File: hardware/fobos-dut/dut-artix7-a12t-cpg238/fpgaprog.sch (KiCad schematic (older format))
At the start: 42 parts, among them J7 0878321420, SW1 SW_DIP_x03, U1 XC7A12T-CPG238

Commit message: Started to rewire the CPG238 into the schematic Split FPGA Power and Programming into two sheets since new FPGA symbol explicitly displays each power pin and is much larger
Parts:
- removed C25: 100uF, Capacitor_SMD:C_1210_3225Metric_Pad1.33x2.70mm_HandSolder, symbol Device:C
- removed C26, C27, C35: 47uF, Capacitor_SMD:C_0603_1608Metric_Pad1.08x0.95mm_HandSolder, symbol Device:C
- removed C28, C29, C36, C37, C38, C39, C40, C41: 4.7uF, Capacitor_SMD:C_0402_1005Metric_Pad0.74x0.62mm_HandSolder, symbol Device:C
- removed C30, C31, C32, C33, C34, C42, C43, C44, C45, C46, C47, C48, C49, C50, C51, C52, C53: .47uF, Capacitor_SMD:C_0402_1005Metric_Pad0.74x0.62mm_HandSolder, symbol Device:C
- U1: footprint (none) -> Package_BGA:Xilinx_CPG238
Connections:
- wire segments 220 -> 106
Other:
- note removed: "BANK0\nE10, R10"
- note removed: "BANK14\nL16, P17, R14, T11, U8, U18, V15"
- note removed: "BANK15\nA16, B13, C10, D17, E14, G18, H15"
- note removed: "BANK34\nL6, M3, P7, R4, T1, V5"
- moved on the sheet: U1B

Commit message: Connected the fixed signals to the FPGA, flexible IO are left unconnected Added 0.1 ohm resistors to the 1V8 and 3V3 power rails, added test points which allow for easy measurement Updated ARTIX7-A12T-CPG238 symbol to make schematic route similarly to the last symbol Connected CFGVBS signal to the 3V3 rail, was previously connected to VCCINT which was a mistake Ran through 7 Series schematic review checklist - 7_Series_Schematic_Review_Recommendations.xlsm Added Xilinx pinout files for the CPG238 package Generated schematic for the csg325 for easy referencing
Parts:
- removed S2: 1825910-6, cerg:Switch_Tactile_THT_6x6mm, symbol cerg:1825910-6
- added C37: 47uF, Capacitor_SMD:C_0603_1608Metric_Pad1.08x0.95mm_HandSolder, symbol Device:C
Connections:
- net labels removed: VCCINT
- wire segments 106 -> 90
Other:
- note added: "BANK0\nG12, V11"
- moved on the sheet: D6, R29, R31, R32, R33, R53, R54, R55, R72, SW1, U1B

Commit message: Added SMA-JOHNSON-142-0701-201 Vertical SMA footprint to CERG lib, added this footprint to the Vcore measurement Re-positioned Power circuitry to the top right quadrant Re-positioned FOBOS connector to the center on the left edge of the board Re-positioned JTAG Connector, Mode switch, and gain control switch to the top left quadrant of the board
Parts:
- J7: symbol dk_Rectangular-Connectors-Headers-Male-Pins:0878321420 -> Connector_Generic:Conn_02x07_Odd_Even
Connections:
- net labels added: MODE_1
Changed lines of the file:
@@
 Connection ~ 3750 4550
 Wire Wire Line
-	4450 4450 4450 4400
-Wire Wire Line
 	5050 4650 5050 4250
 Wire Wire Line
@@
 	5250 4850 5250 4350
 $Comp
-L dk_Rectangular-Connectors-Headers-Male-Pins:0878321420 J?
+L Connector_Generic:Conn_02x07_Odd_Even J?
 U 1 1 600F5844
 P 4100 4750
@@
 Wire Wire Line
 	3750 5050 3900 5050
-Wire Wire Line
-	4300 4850 5250 4850
-Wire Wire Line
-	4300 4750 5150 4750
-Wire Wire Line
-	4300 4650 5050 4650
-Wire Wire Line
-	4300 4450 4450 4450
 $Comp
 L cerg:SW_DIP_x03 SW1
@@
 	5150 4450 5900 4450
 Wire Wire Line
-	5900 4550 4300 4550
-Wire Wire Line
 	5350 4650 5900 4650
 Wire Wire Line
@@
 	1    0    0    -1
 $EndComp
+Text Label 5450 3950 0    50   ~ 0
+MODE_1
+Wire Wire Line
+	4400 4450 4450 4450
+Wire Wire Line
+	4450 4450 4450 4400
+Wire Wire Line
+	4400 4550 5900 4550
+Wire Wire Line
+	5050 4650 4400 4650
+Wire Wire Line
+	5150 4750 4400 4750
+Wire Wire Line
+	5250 4850 4400 4850
 $EndSCHEMATC

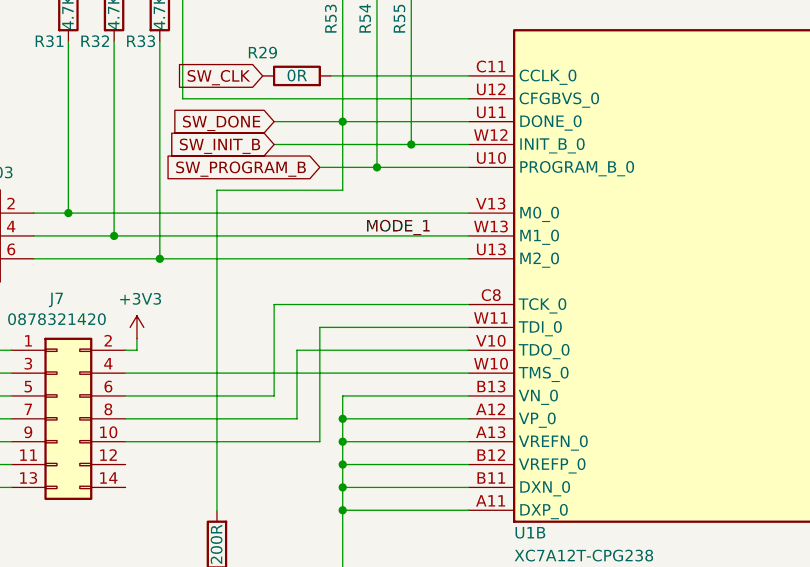
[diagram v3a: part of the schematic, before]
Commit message: updated library ref for diode and FET, placed target connector and some parts
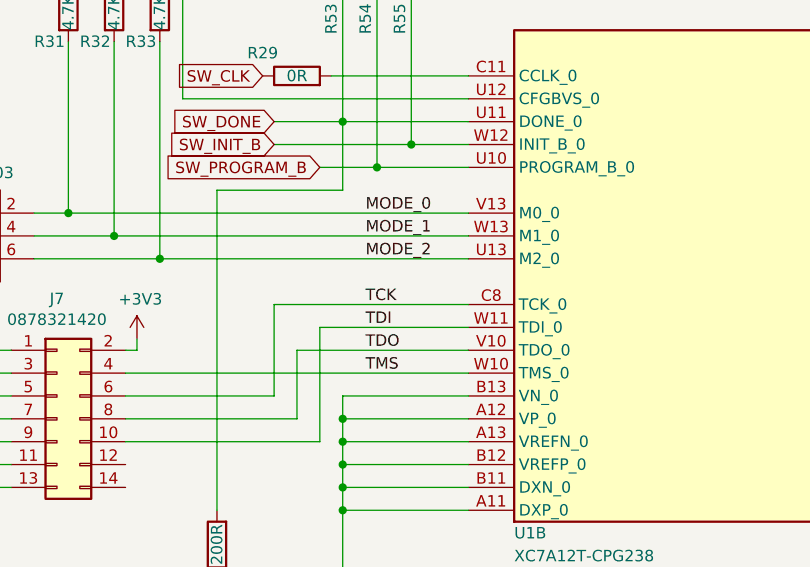
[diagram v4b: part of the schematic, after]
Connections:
- net MODE_2: now reaches R33.2, SW1.6, U1.U13 (M2_0)
- net MODE_0: now reaches R31.2, SW1.2, U1.V13 (M0_0)
- net TDI: now reaches J7.10 (Pin_10), U1.W11 (TDI_0)
- net TMS: now reaches J7.4 (Pin_4), U1.W10 (TMS_0)
- net TCK: now reaches J7.6 (Pin_6), U1.C8 (TCK_0)
- net TDO: now reaches J7.8 (Pin_8), U1.V10 (TDO_0)
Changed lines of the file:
@@
 Wire Wire Line
 	5250 4850 4400 4850
+Text Label 5450 3850 0    50   ~ 0
+MODE_0
+Text Label 5450 4050 0    50   ~ 0
+MODE_2
+Text Label 5450 4250 0    50   ~ 0
+TCK
+Text Label 5450 4350 0    50   ~ 0
+TDI
+Text Label 5450 4450 0    50   ~ 0
+TDO
+Text Label 5450 4550 0    50   ~ 0
+TMS
 $EndSCHEMATC

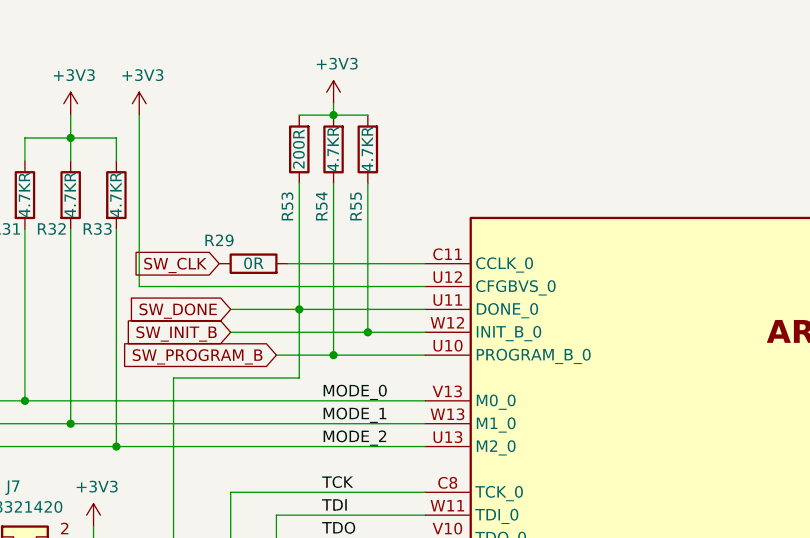
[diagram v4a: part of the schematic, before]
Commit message: few layout alignments incl space around FPGA
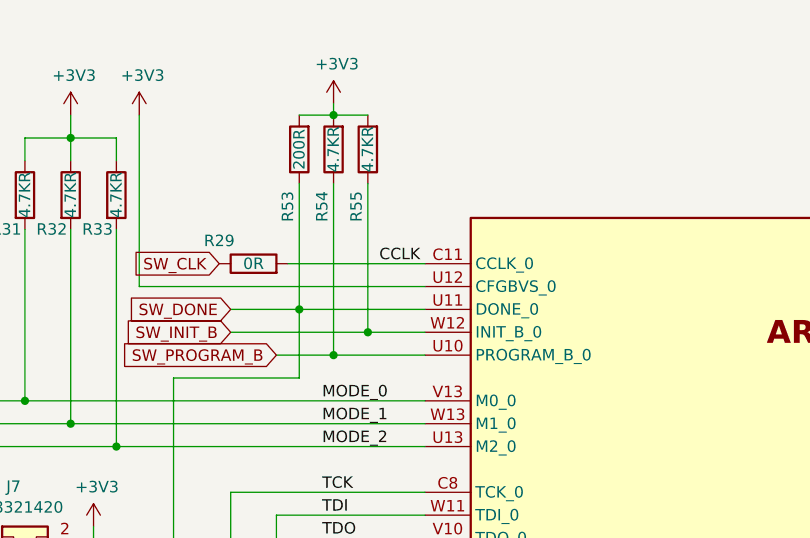
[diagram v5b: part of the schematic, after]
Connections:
- net CCLK: now reaches R29.2, U1.C11 (CCLK_0)
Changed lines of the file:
@@
 Text Label 5450 4550 0    50   ~ 0
 TMS
+Text Label 5700 3250 0    50   ~ 0
+CCLK
 $EndSCHEMATC

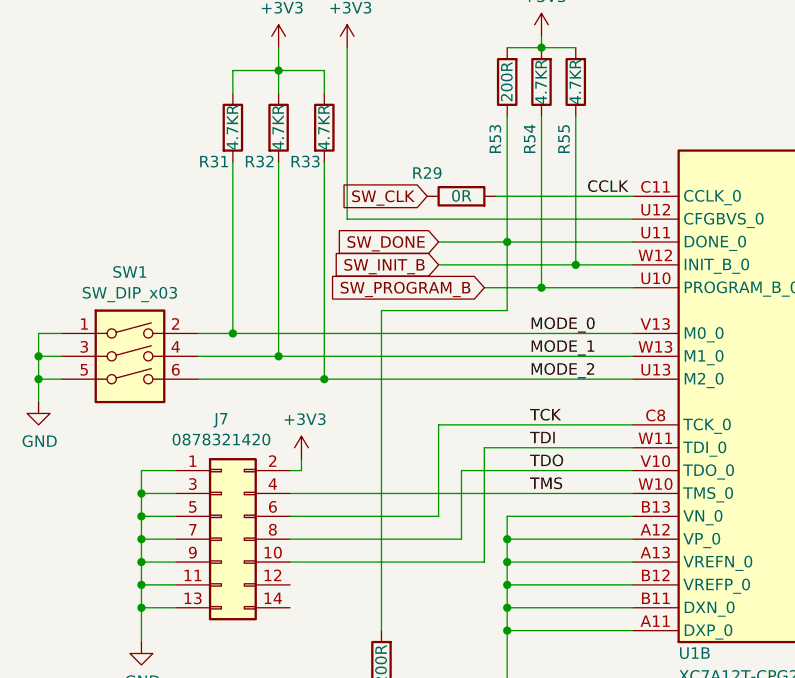
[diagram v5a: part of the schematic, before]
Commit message: All signals routed, need to route power
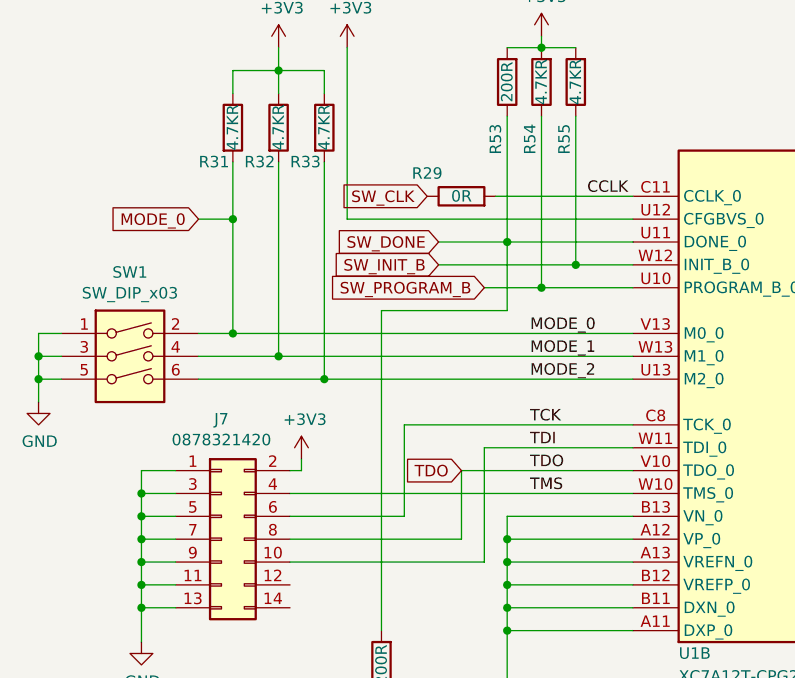
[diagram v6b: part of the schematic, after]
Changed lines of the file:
@@
 $EndComp
 Wire Wire Line
-	4150 3100 4150 3850
+	4150 3100 4150 3350
 Connection ~ 4150 3850
 Wire Wire Line
@@
 Connection ~ 3750 4550
 Wire Wire Line
-	5050 4650 5050 4250
+	4900 4650 4900 4250
 Wire Wire Line
 	5150 4750 5150 4450
@@
 	7700 5400 7700 5500
 Wire Wire Line
-	5050 4250 5900 4250
+	4900 4250 5900 4250
 Wire Wire Line
 	5250 4350 5900 4350
@@
 	4400 4550 5900 4550
 Wire Wire Line
-	5050 4650 4400 4650
+	4900 4650 4400 4650
 Wire Wire Line
 	5150 4750 4400 4750
@@
 Text Label 5700 3250 0    50   ~ 0
 CCLK
+Text GLabel 5150 4450 0    50   Input ~ 0
+TDO
+Text GLabel 4000 3350 0    50   Input ~ 0
+MODE_0
+Wire Wire Line
+	4000 3350 4150 3350
+Connection ~ 4150 3350
+Wire Wire Line
+	4150 3350 4150 3850
 $EndSCHEMATC
